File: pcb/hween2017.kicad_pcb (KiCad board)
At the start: 2 copper layers, 86.4 x 66 mm, 16 parts, among them J1 BATTERY, J2 JTAG, U1 HV509, U2 MSP430FR2100IPW

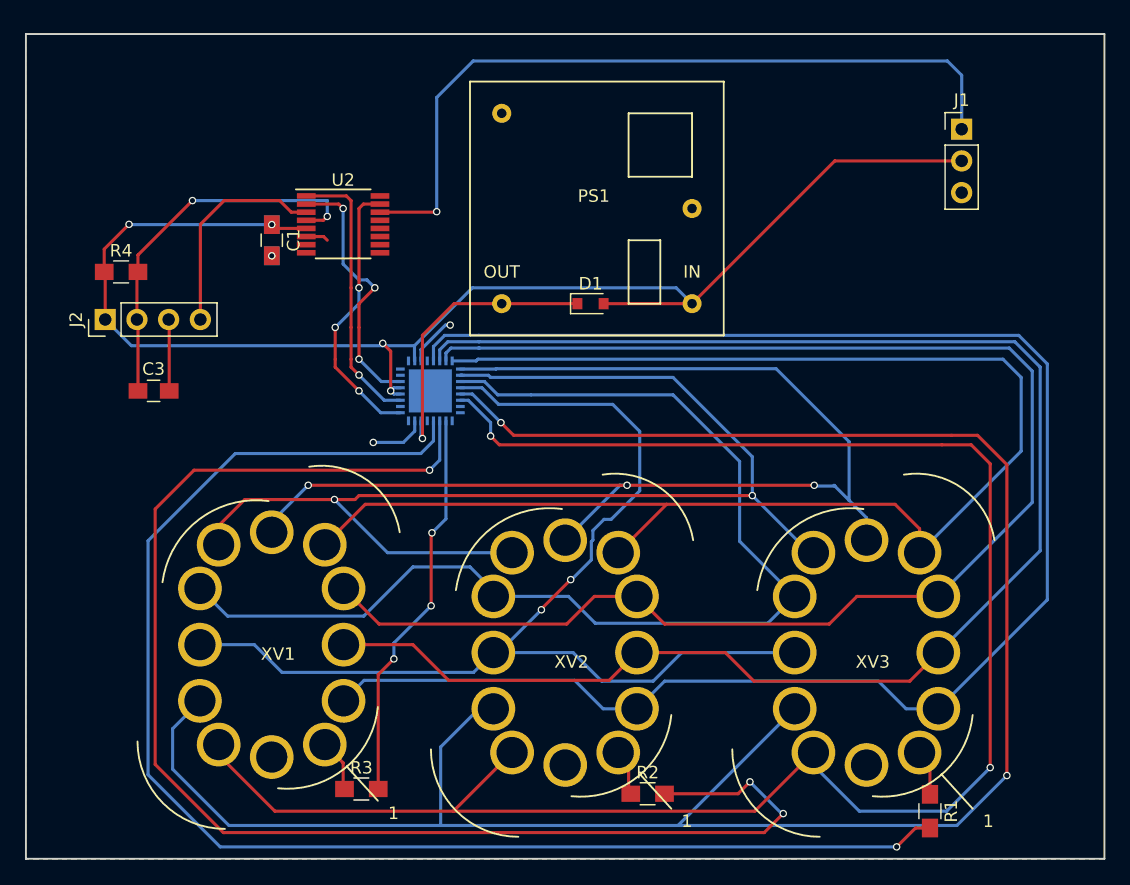
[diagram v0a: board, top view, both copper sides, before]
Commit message: Add new PCB changes and a stencil STL file.
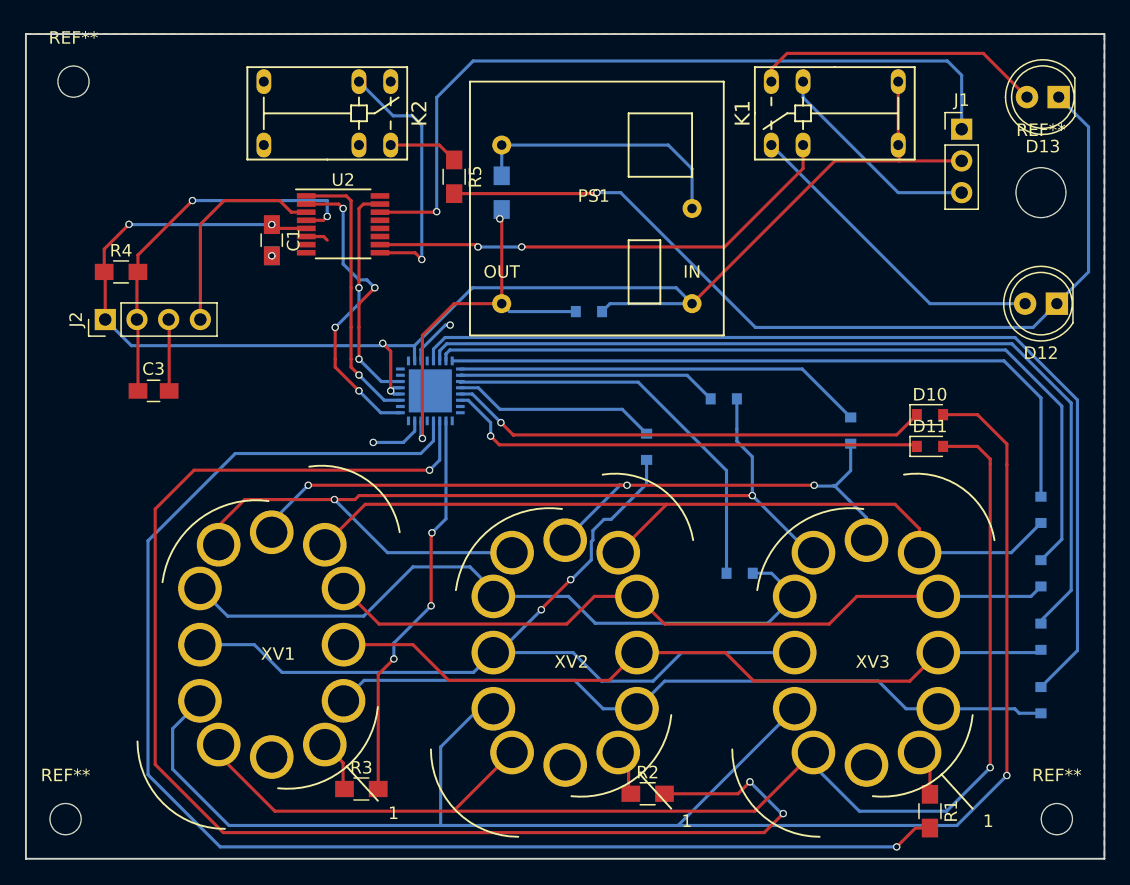
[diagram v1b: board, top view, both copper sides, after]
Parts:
- added D10: D, Diodes_SMD:D_0805, F.Cu at (110.5, 92.7)
- added D11: D, Diodes_SMD:D_0805, F.Cu at (110.5, 95.2)
- added D12: LED, LEDs:LED_D5.0mm, F.Cu at (120.7, 83.8)
- added D13: LED, LEDs:LED_D5.0mm, F.Cu at (120.8, 67.3)
- added D2: D, Diodes_SMD:D_0805, B.Cu at (119.4, 115.6)
- added D3: D, Diodes_SMD:D_0805, B.Cu at (119.4, 110.5)
- added D4: D, Diodes_SMD:D_0805, B.Cu at (119.4, 105.4)
- added D5: D, Diodes_SMD:D_0805, B.Cu at (119.4, 100.3)
- added D6: D, Diodes_SMD:D_0805, B.Cu at (104.1, 94.0)
- added D7: D, Diodes_SMD:D_0805, B.Cu at (94.0, 91.4)
- added D8: D, Diodes_SMD:D_0805, B.Cu at (95.2, 105.4)
- added D9: D, Diodes_SMD:D_0805, B.Cu at (87.8, 95.3)
- added K1: SY-3W-K, halloween:Fujitsu_Relay_SY-3W-K_SPDT_12.5x7.4, F.Cu at (102.9, 68.6)
- added K2: SY-3W-K, halloween:Fujitsu_Relay_SY-3W-K_SPDT_12.5x7.4, F.Cu at (62.2, 68.6)
- added R5: 1 k, Resistors_SMD:R_0805_HandSoldering, F.Cu at (72.4, 73.7)
- added R6: 100k, Resistors_SMD:R_0805_HandSoldering, B.Cu at (76.2, 74.9)
- added REF**: MountingHole_4mm, Mounting_Holes:MountingHole_4mm, F.Cu at (119.4, 74.9)
- added REF**: MountingHole_2.5mm, Mounting_Holes:MountingHole_2.5mm, F.Cu at (120.7, 125.1)
- added REF**: MountingHole_2.5mm, Mounting_Holes:MountingHole_2.5mm, F.Cu at (41.3, 125.1)
- added REF**: MountingHole_2.5mm, Mounting_Holes:MountingHole_2.5mm, F.Cu at (41.9, 66.0)
- D1: moved to B.Cu
- moved D1 0.65 mm to (83.2, 84.5)
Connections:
- U1 pad 1: /if_6 -> Net-(D6-Pad1)
- U1 pad 2: /if_5 -> Net-(D7-Pad1)
- U1 pad 29: /if_0 -> Net-(D2-Pad1)
- U1 pad 3: /if_4 -> Net-(D8-Pad1)
- U1 pad 30: /if_9 -> Net-(D3-Pad1)
- U1 pad 31: /if_8 -> Net-(D4-Pad1)
- U1 pad 32: /if_7 -> Net-(D5-Pad1)
- U1 pad 4: /if_3 -> Net-(D9-Pad1)
- U1 pad 5: /if_2 -> Net-(D10-Pad1)
- U1 pad 6: /if_1 -> Net-(D11-Pad1)
- U2 pad 10: Net-(U2-Pad10) -> L_IN
- U2 pad 9: Net-(U2-Pad9) -> L_OUT
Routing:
- net Net-(D2-Pad1): track 0.00 -> 79.2 mm
- net /if_0: track 134.0 -> 59.5 mm
- net Net-(D3-Pad1): track 0.00 -> 72.2 mm
- net Net-(D12-Pad1): track 0.00 -> 72.1 mm, vias 0 -> 1
- net /if_9: track 128.0 -> 59.9 mm
- net Net-(D4-Pad1): track 0.00 -> 64.9 mm
- net /if_8: track 121.3 -> 60.1 mm
- net Net-(D5-Pad1): track 0.00 -> 56.3 mm
- net /if_7: track 120.8 -> 67.9 mm
- net /if_1: track 146.6 -> 106.0 mm, vias 2 -> 1
- net Earth: track 16.1 -> 54.9 mm
- net Net-(D11-Pad1): track 0.00 -> 38.7 mm, vias 0 -> 1
- net Net-(D10-Pad1): track 0.00 -> 38.6 mm, vias 0 -> 1
- net L_IN: track 0.00 -> 38.4 mm, vias 0 -> 2
- net /if_2: track 172.7 -> 134.3 mm, vias 2 -> 1
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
